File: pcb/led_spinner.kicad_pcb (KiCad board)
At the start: 2 copper layers, 48.3 x 48.3 mm, 43 parts, among them CON1 AVR-ISP-6, J1 SERIAL, J2 SPARE, J3 TILT, SW1 SW_PUSH_ALT, U1 ATMEGA48_88_168_328P-32SMD

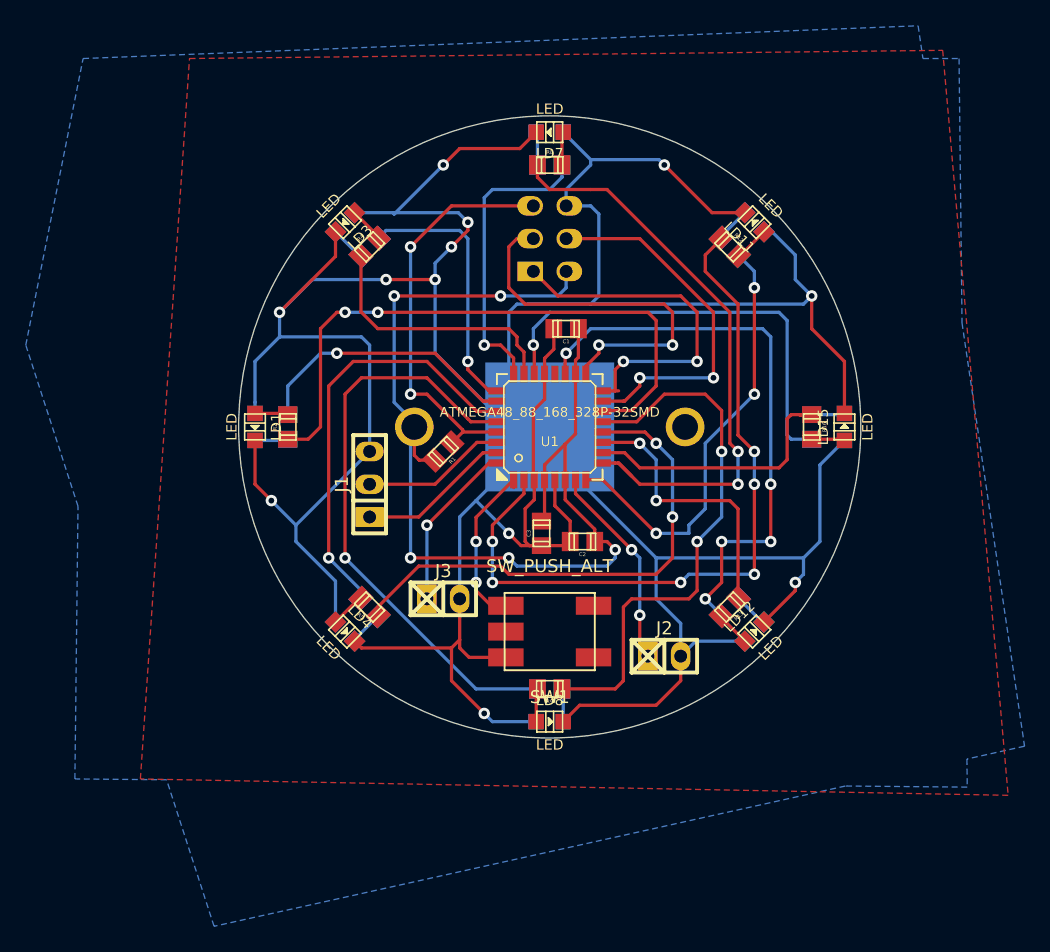
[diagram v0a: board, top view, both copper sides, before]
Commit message: Tidy up the front silkscreen. (Remove off-board silkscreen. Remove overlaps. Add useful connector names.)
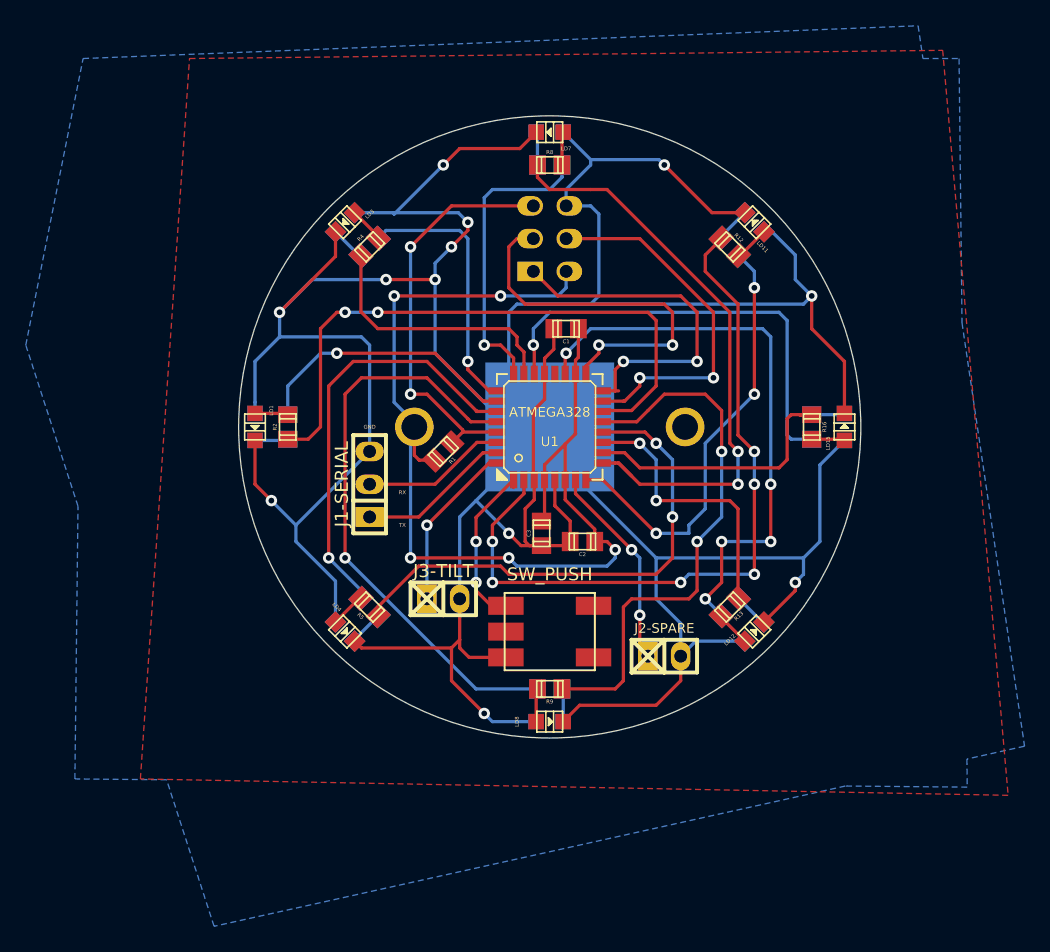
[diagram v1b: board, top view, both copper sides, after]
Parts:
- removed J2: SPARE, w_pin_strip:pin_socket_2
- added J2-SPARE: SPARE, w_pin_strip:pin_socket_2, F.Cu at (203.2, 124.5)
- SW1: value SW_PUSH_ALT -> SW_PUSH
- U1: value ATMEGA48_88_168_328P-32SMD -> ATMEGA328
- renumbered J1 to J1-SERIAL, J3 to J3-TILT
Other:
- board text added: "GND"
- board text added: "RX"
- board text added: "TX"
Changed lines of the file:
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@@
     (links 77)
     (no_connects 0)
-    (area 170.129999 82.499999 218.490001 130.860001)
+    (area 153.67 75.565 231.140001 145.415001)
     (thickness 1.6)
-    (drawings 7)
+    (drawings 10)
     (tracks 461)
     (zones 0)
@@
     (descr "Pin socket 3pin")
     (tags "CONN DEV")
-    (fp_text reference J1 (at 0 -2.159 90) (layer F.SilkS)
+    (fp_text reference J1-SERIAL (at 0 -2.159 90) (layer F.SilkS)
       (effects (font (size 1.016 1.016) (thickness 0.2032)))
     )
@@
     (descr "Pin socket 2pin")
     (tags "CONN DEV")
-    (fp_text reference J2 (at 0 -2.159) (layer F.SilkS)
-      (effects (font (size 1.016 1.016) (thickness 0.2032)))
+    (fp_text reference J2-SPARE (at 0 -2.159) (layer F.SilkS)
+      (effects (font (size 0.75 0.75) (thickness 0.125)))
     )
     (fp_text value SPARE (at 0.254 -3.556) (layer F.SilkS) hide
@@
     (descr "Pin socket 2pin")
     (tags "CONN DEV")
-    (fp_text reference J3 (at 0 -2.159) (layer F.SilkS)
+    (fp_text reference J3-TILT (at 0 -2.159) (layer F.SilkS)
       (effects (font (size 1.016 1.016) (thickness 0.2032)))
     )
@@
     (at 171.45 106.68 270)
     (descr "SMD LED, 0805")
-    (fp_text reference LD1 (at 0 -1.651 270) (layer F.SilkS)
-      (effects (font (size 0.8001 0.8001) (thickness 0.14986)))
-    )
-    (fp_text value LED (at 0 1.80086 270) (layer F.SilkS)
+    (fp_text reference LD1 (at -1.27 -1.27 270) (layer F.SilkS)
+      (effects (font (size 0.3 0.3) (thickness 0.075)))
+    )
+    (fp_text value LED (at 0 1.80086 270) (layer F.SilkS) hide
       (effects (font (size 0.8001 0.8001) (thickness 0.14986)))
     )
@@
     (at 178.435 90.805 225)
     (descr "SMD LED, 0805")
-    (fp_text reference LD3 (at 0 -1.651 225) (layer F.SilkS)
-      (effects (font (size 0.8001 0.8001) (thickness 0.14986)))
-    )
-    (fp_text value LED (at 0 1.80086 225) (layer F.SilkS)
+    (fp_text reference LD3 (at -1.796051 -0.898026 225) (layer F.SilkS)
+      (effects (font (size 0.3 0.3) (thickness 0.075)))
+    )
+    (fp_text value LED (at 0 1.80086 225) (layer F.SilkS) hide
       (effects (font (size 0.8001 0.8001) (thickness 0.14986)))
     )
@@
     (at 178.435 122.555 315)
     (descr "SMD LED, 0805")
-    (fp_text reference LD4 (at 0 -1.651 315) (layer F.SilkS)
-      (effects (font (size 0.8001 0.8001) (thickness 0.14986)))
-    )
-    (fp_text value LED (at 0 1.80086 315) (layer F.SilkS)
+    (fp_text reference LD4 (at -1.796051 -0.898026 315) (layer F.SilkS)
+      (effects (font (size 0.3 0.3) (thickness 0.075)))
+    )
+    (fp_text value LED (at 0 1.80086 315) (layer F.SilkS) hide
       (effects (font (size 0.8001 0.8001) (thickness 0.14986)))
     )
@@
     (at 194.31 83.82 180)
     (descr "SMD LED, 0805")
-    (fp_text reference LD7 (at 0 -1.651 180) (layer F.SilkS)
-      (effects (font (size 0.8001 0.8001) (thickness 0.14986)))
-    )
-    (fp_text value LED (at 0 1.80086 180) (layer F.SilkS)
+    (fp_text reference LD7 (at -1.27 -1.27 180) (layer F.SilkS)
+      (effects (font (size 0.3 0.3) (thickness 0.075)))
+    )
+    (fp_text value LED (at 0 1.80086 180) (layer F.SilkS) hide
       (effects (font (size 0.8001 0.8001) (thickness 0.14986)))
     )
@@
     (at 194.31 129.54)
     (descr "SMD LED, 0805")
-    (fp_text reference LD8 (at 0 -1.651) (layer F.SilkS)
-      (effects (font (size 0.8001 0.8001) (thickness 0.14986)))
-    )
-    (fp_text value LED (at 0 1.80086) (layer F.SilkS)
+    (fp_text reference LD8 (at -2.54 0 270) (layer F.SilkS)
+      (effects (font (size 0.3 0.3) (thickness 0.075)))
+    )
+    (fp_text value LED (at 0 1.80086) (layer F.SilkS) hide
       (effects (font (size 0.8001 0.8001) (thickness 0.14986)))
     )
@@
     (at 210.185 90.805 135)
     (descr "SMD LED, 0805")
-    (fp_text reference LD11 (at 0 -1.651 135) (layer F.SilkS)
-      (effects (font (size 0.8001 0.8001) (thickness 0.14986)))
-    )
-    (fp_text value LED (at 0 1.80086 135) (layer F.SilkS)
+    (fp_text reference LD11 (at -1.796051 -0.898026 135) (layer F.SilkS)
+      (effects (font (size 0.3 0.3) (thickness 0.075)))
+    )
+    (fp_text value LED (at 0 1.80086 135) (layer F.SilkS) hide
       (effects (font (size 0.8001 0.8001) (thickness 0.14986)))
     )
@@
     (at 210.185 122.555 45)
     (descr "SMD LED, 0805")
-    (fp_text reference LD12 (at 0 -1.651 45) (layer F.SilkS)
-      (effects (font (size 0.8001 0.8001) (thickness 0.14986)))
-    )
-    (fp_text value LED (at 0 1.80086 45) (layer F.SilkS)
+    (fp_text reference LD12 (at -1.796051 -0.898026 45) (layer F.SilkS)
+      (effects (font (size 0.3 0.3) (thickness 0.075)))
+    )
+    (fp_text value LED (at 0 1.80086 45) (layer F.SilkS) hide
       (effects (font (size 0.8001 0.8001) (thickness 0.14986)))
     )
@@
     (at 217.17 106.68 90)
     (descr "SMD LED, 0805")
-    (fp_text reference LD15 (at 0 -1.651 90) (layer F.SilkS)
-      (effects (font (size 0.8001 0.8001) (thickness 0.14986)))
-    )
-    (fp_text value LED (at 0 1.80086 90) (layer F.SilkS)
+    (fp_text reference LD15 (at -1.27 -1.27 90) (layer F.SilkS)
+      (effects (font (size 0.3 0.3) (thickness 0.075)))
+    )
+    (fp_text value LED (at 0 1.80086 90) (layer F.SilkS) hide
       (effects (font (size 0.8001 0.8001) (thickness 0.14986)))
     )
@@
   (module OMRON-PUSH-BUTTON-B3SN-3112P:OMRON-PUSH-BUTTON-B3SN-3112P (layer F.Cu)
     (at 194.31 122.555 180)
-    (fp_text reference SW1 (at 0 -5.08 180) (layer F.SilkS)
+    (fp_text reference SW1 (at 0 -5.08 180) (layer F.SilkS) hide
       (effects (font (size 1 1) (thickness 0.15)))
     )
-    (fp_text value SW_PUSH_ALT (at 0 5.08 180) (layer F.SilkS)
+    (fp_text value SW_PUSH (at 0 4.445 180) (layer F.SilkS)
       (effects (font (size 1 1) (thickness 0.15)))
     )
@@
       (effects (font (size 0.7493 0.7493) (thickness 0.14986)))
     )
-    (fp_text value ATMEGA48_88_168_328P-32SMD (at 0 -1.143) (layer F.SilkS)
+    (fp_text value ATMEGA328 (at 0 -1.143) (layer F.SilkS)
       (effects (font (size 0.7493 0.7493) (thickness 0.14986)))
     )
@@
     )
   )
+  (gr_text GND (at 180.34 106.68) (layer F.SilkS)
+    (effects (font (size 0.3 0.3) (thickness 0.075)))
+  )
+  (gr_text RX (at 182.88 111.76) (layer F.SilkS)
+    (effects (font (size 0.3 0.3) (thickness 0.075)))
+  )
+  (gr_text TX (at 182.88 114.3) (layer F.SilkS)
+    (effects (font (size 0.3 0.3) (thickness 0.075)))
+  )
   (gr_line (start 194.31 106.68) (end 175.895 88.265) (angle 90) (layer Dwgs.User) (width 0.2))

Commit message: Fix up back silkscreen.
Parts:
- renumbered CON1 to CON1_ICSP
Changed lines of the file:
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@@
     (descr "Pin socket 3x2pin")
     (tags "CONN DEV")
-    (fp_text reference CON1 (at 0 3.81 90) (layer B.SilkS)
+    (fp_text reference CON1_ICSP (at 0 3.81 90) (layer B.SilkS)
       (effects (font (size 1.016 1.016) (thickness 0.2032)) (justify mirror))
     )
@@
     (at 217.17 106.68 270)
     (descr "SMD LED, 0805")
-    (fp_text reference LD2 (at 0 1.651 270) (layer B.SilkS)
-      (effects (font (size 0.8001 0.8001) (thickness 0.14986)) (justify mirror))
-    )
-    (fp_text value LED (at 0 -1.80086 270) (layer B.SilkS)
+    (fp_text reference LD2 (at -1.27 1.27 270) (layer B.SilkS)
+      (effects (font (size 0.3 0.3) (thickness 0.075)) (justify mirror))
+    )
+    (fp_text value LED (at 0 -1.80086 270) (layer B.SilkS) hide
       (effects (font (size 0.8001 0.8001) (thickness 0.14986)) (justify mirror))
     )
@@
     (at 210.185 90.805 315)
     (descr "SMD LED, 0805")
-    (fp_text reference LD5 (at 0 1.651 315) (layer B.SilkS)
-      (effects (font (size 0.8001 0.8001) (thickness 0.14986)) (justify mirror))
-    )
-    (fp_text value LED (at 0 -1.80086 315) (layer B.SilkS)
+    (fp_text reference LD5 (at 1.796051 0.898026 315) (layer B.SilkS)
+      (effects (font (size 0.3 0.3) (thickness 0.075)) (justify mirror))
+    )
+    (fp_text value LED (at 0 -1.80086 315) (layer B.SilkS) hide
       (effects (font (size 0.8001 0.8001) (thickness 0.14986)) (justify mirror))
     )
@@
     (at 210.185 122.555 225)
     (descr "SMD LED, 0805")
-    (fp_text reference LD6 (at 0 1.651 225) (layer B.SilkS)
-      (effects (font (size 0.8001 0.8001) (thickness 0.14986)) (justify mirror))
-    )
-    (fp_text value LED (at 0 -1.80086 225) (layer B.SilkS)
+    (fp_text reference LD6 (at -1.796051 0.898026 225) (layer B.SilkS)
+      (effects (font (size 0.3 0.3) (thickness 0.075)) (justify mirror))
+    )
+    (fp_text value LED (at 0 -1.80086 225) (layer B.SilkS) hide
       (effects (font (size 0.8001 0.8001) (thickness 0.14986)) (justify mirror))
     )
@@
     (at 194.31 83.82)
     (descr "SMD LED, 0805")
-    (fp_text reference LD9 (at 0 1.651) (layer B.SilkS)
-      (effects (font (size 0.8001 0.8001) (thickness 0.14986)) (justify mirror))
-    )
-    (fp_text value LED (at 0 -1.80086) (layer B.SilkS)
+    (fp_text reference LD9 (at 1.27 1.27) (layer B.SilkS)
+      (effects (font (size 0.3 0.3) (thickness 0.075)) (justify mirror))
+    )
+    (fp_text value LED (at 0 -1.80086) (layer B.SilkS) hide
       (effects (font (size 0.8001 0.8001) (thickness 0.14986)) (justify mirror))
     )
@@
     (at 194.31 129.54 180)
     (descr "SMD LED, 0805")
-    (fp_text reference LD10 (at 0 1.651 180) (layer B.SilkS)
-      (effects (font (size 0.8001 0.8001) (thickness 0.14986)) (justify mirror))
-    )
-    (fp_text value LED (at 0 -1.80086 180) (layer B.SilkS)
+    (fp_text reference LD10 (at -1.27 1.27 180) (layer B.SilkS)
+      (effects (font (size 0.3 0.3) (thickness 0.075)) (justify mirror))
+    )
+    (fp_text value LED (at 0 -1.80086 180) (layer B.SilkS) hide
       (effects (font (size 0.8001 0.8001) (thickness 0.14986)) (justify mirror))
     )
@@
     (at 178.435 90.805 45)
     (descr "SMD LED, 0805")
-    (fp_text reference LD13 (at 0 1.651 45) (layer B.SilkS)
-      (effects (font (size 0.8001 0.8001) (thickness 0.14986)) (justify mirror))
-    )
-    (fp_text value LED (at 0 -1.80086 45) (layer B.SilkS)
+    (fp_text reference LD13 (at 1.796051 0.898026 45) (layer B.SilkS)
+      (effects (font (size 0.3 0.3) (thickness 0.075)) (justify mirror))
+    )
+    (fp_text value LED (at 0 -1.80086 45) (layer B.SilkS) hide
       (effects (font (size 0.8001 0.8001) (thickness 0.14986)) (justify mirror))
     )
@@
     (at 178.435 122.555 135)
     (descr "SMD LED, 0805")
-    (fp_text reference LD14 (at 0 1.651 135) (layer B.SilkS)
-      (effects (font (size 0.8001 0.8001) (thickness 0.14986)) (justify mirror))
-    )
-    (fp_text value LED (at 0 -1.80086 135) (layer B.SilkS)
+    (fp_text reference LD14 (at -1.796051 0.898026 135) (layer B.SilkS)
+      (effects (font (size 0.3 0.3) (thickness 0.075)) (justify mirror))
+    )
+    (fp_text value LED (at 0 -1.80086 135) (layer B.SilkS) hide
       (effects (font (size 0.8001 0.8001) (thickness 0.14986)) (justify mirror))
     )
@@
     (at 171.45 106.68 90)
     (descr "SMD LED, 0805")
-    (fp_text reference LD16 (at 0 1.651 90) (layer B.SilkS)
-      (effects (font (size 0.8001 0.8001) (thickness 0.14986)) (justify mirror))
-    )
-    (fp_text value LED (at 0 -1.80086 90) (layer B.SilkS)
-      (effects (font (size 0.8001 0.8001) (thickness 0.14986)) (justify mirror))
-    )
+    (fp_text reference LD16 (at 1.27 1.27 90) (layer B.SilkS)
+      (effects (font (size 0.3 0.3) (thickness 0.075)) (justify mirror))
+    )
+    (fp_text value LED (at 0 -1.80086 90) (layer B.SilkS) hide
+      (effects (font (size 0.8001 0.8001) (thickness 0.14986)) (justify mirror))
+    )

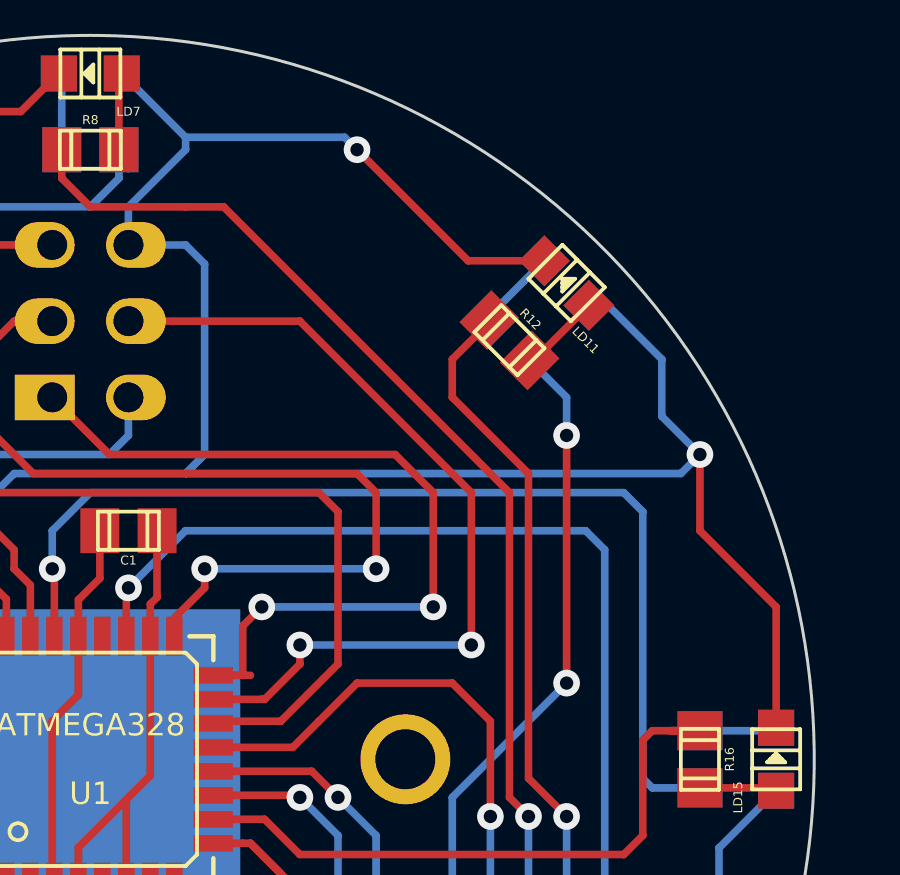
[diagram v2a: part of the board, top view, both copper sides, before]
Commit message: Add project and version ID text.
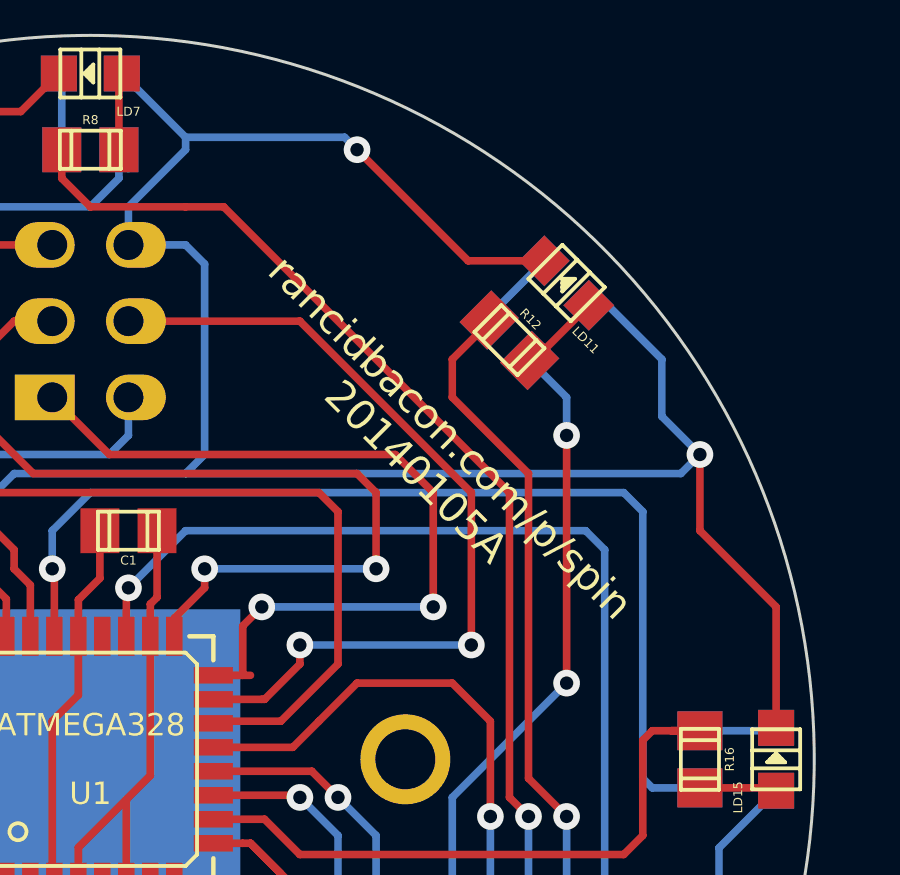
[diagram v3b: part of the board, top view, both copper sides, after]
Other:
- board text added: "rancidbacon.com/p/spin 20140105A"
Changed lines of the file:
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@@
     (area 153.67 75.565 231.140001 145.415001)
     (thickness 1.6)
-    (drawings 10)
+    (drawings 11)
     (tracks 461)
     (zones 0)
@@
     )
   )
+  (gr_text "rancidbacon.com/p/spin\n20140105A" (at 205.74 96.52 315) (layer F.SilkS)
+    (effects (font (size 1 1) (thickness 0.25)))
+  )
   (gr_text GND (at 180.34 106.68) (layer F.SilkS)
